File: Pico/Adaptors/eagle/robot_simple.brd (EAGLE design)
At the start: 75.4 x 35.6 mm, 30 parts, among them SW1 3010010P1,MS-22D18,JS202011CQN, U3 MAX1555

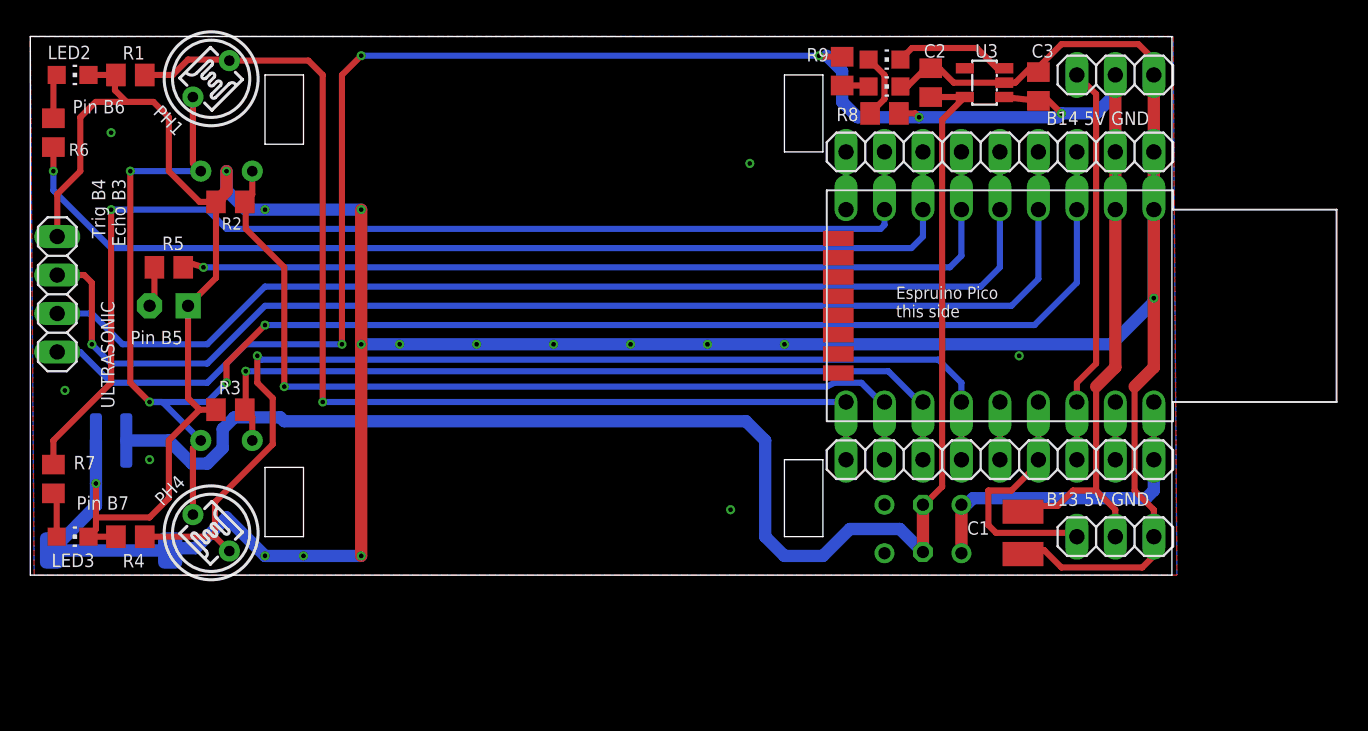
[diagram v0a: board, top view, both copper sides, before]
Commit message: rotate ultrasonic, add fast charge
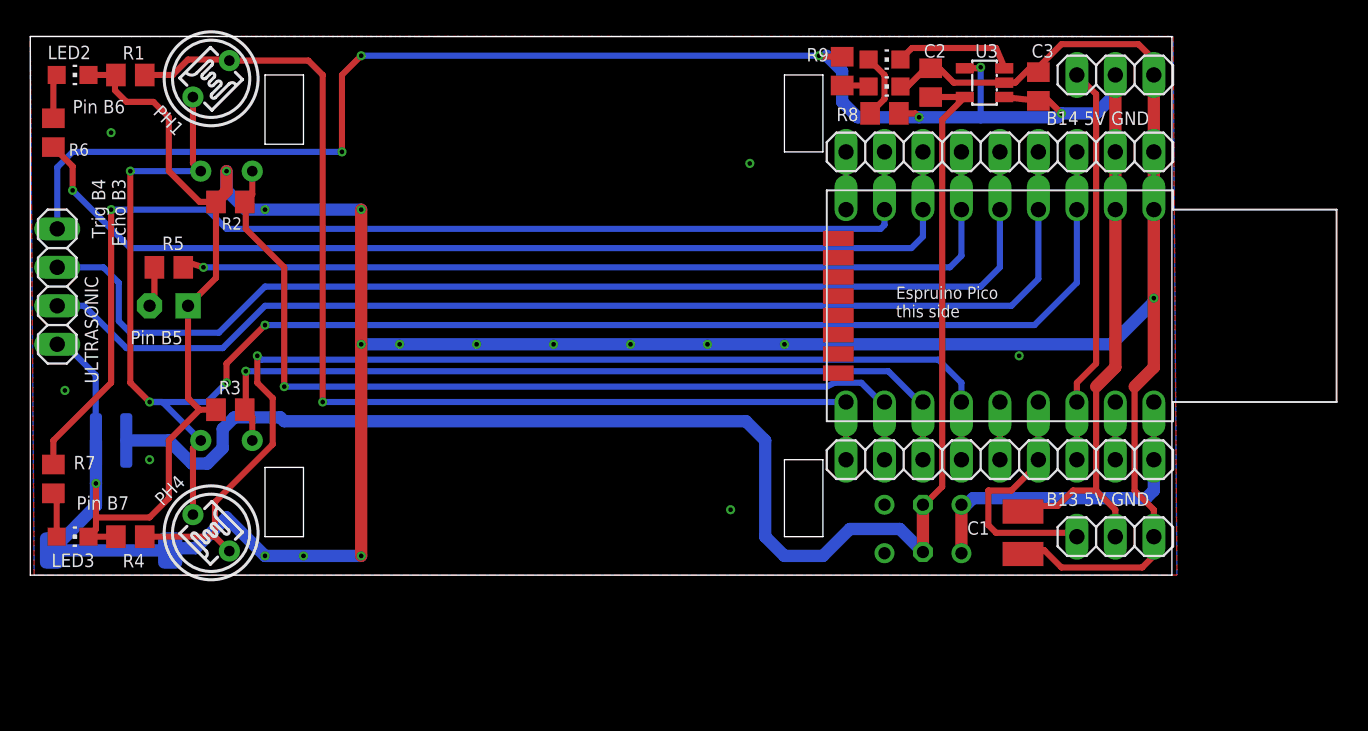
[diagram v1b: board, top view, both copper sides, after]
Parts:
- moved ULTRASONIC 0.51 mm to (1.78, 19.1), turned to 270 degrees
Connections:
- net 5V: now also U3.4
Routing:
- net 5V: track 139.2 -> 133.4 mm, vias 5 -> 6
- net SONIC_ECHO: track 80.3 -> 76.2 mm, vias 1 -> 0
- net SONIC_TRIG: track 72.8 -> 74.9 mm
- net GND: track 249.3 -> 247.8 mm
- net LED2: track 67.7 -> 67.0 mm
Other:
- board text added: "v1.1"
- board text removed: "v1.0"
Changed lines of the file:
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@@
 <text x="4.064" y="26.162" size="0.889" layer="21" rot="R270">Trig B4
 Echo B3</text>
-<text x="40.894" y="25.4" size="0.889" layer="22" rot="MR180">v1.0</text>
+<text x="40.894" y="25.4" size="0.889" layer="22" rot="MR180">v1.1</text>
 </plain>
 <attributes>
@@
 <attribute name="NAME" x="6.096" y="0.508" size="0.889" layer="25"/>
 </element>
-<element name="ULTRASONIC" library="pinhead" package="1X04" value="" x="1.778" y="18.542" smashed="yes" rot="R90">
-<attribute name="NAME" x="5.552515625" y="11.012928125" size="0.889" layer="25" ratio="10" rot="R90"/>
-<attribute name="VALUE" x="4.952996875" y="13.462" size="1.27" layer="27" rot="R90"/>
+<element name="ULTRASONIC" library="pinhead" package="1X04" value="" x="1.778" y="19.05" smashed="yes" rot="R270">
+<attribute name="NAME" x="3.591484375" y="19.721071875" size="0.889" layer="25" ratio="10" rot="R270"/>
+<attribute name="VALUE" x="-1.396996875" y="24.13" size="1.27" layer="27" rot="R270"/>
 </element>
 <element name="J1" library="OPL5" package="2P-SMD-2.0-90D" value="" x="5.334" y="3.81" smashed="yes" rot="MR0"/>
@@
 <wire x1="5.588" y1="32.004" x2="5.588" y2="32.954" width="0.4064" layer="1"/>
 <wire x1="5.588" y1="32.954" x2="5.654" y2="33.02" width="0.4064" layer="1"/>
-<wire x1="1.778" y1="22.352" x2="1.778" y2="25.146" width="0.4064" layer="1"/>
-<wire x1="1.778" y1="25.146" x2="3.302" y2="26.67" width="0.4064" layer="1"/>
-<wire x1="3.302" y1="26.67" x2="3.302" y2="30.226" width="0.4064" layer="1"/>
-<wire x1="3.302" y1="30.226" x2="4.318" y2="31.242" width="0.4064" layer="1"/>
-<wire x1="4.318" y1="31.242" x2="6.35" y2="31.242" width="0.4064" layer="1"/>
 <wire x1="4.334" y1="8.89" x2="4.334" y2="6.053" width="0.8128" layer="16"/>
 <wire x1="4.334" y1="6.053" x2="4.334" y2="4.588" width="0.8128" layer="16"/>
@@
 <via x="7.874" y="7.62" extent="1-16" drill="0.3048"/>
 <via x="5.334" y="29.21" extent="1-16" drill="0.3048"/>
+<wire x1="1.778" y1="15.24" x2="2.286" y2="15.24" width="0.4064" layer="16"/>
+<wire x1="2.286" y1="15.24" x2="4.318" y2="13.208" width="0.4064" layer="16"/>
+<wire x1="4.318" y1="13.208" x2="4.318" y2="6.096" width="0.4064" layer="16"/>
 </signal>
 <signal name="N$5">
@@
 <wire x1="58.42" y1="30.48" x2="58.674" y2="30.226" width="0.4064" layer="1"/>
 <via x="58.674" y="30.226" extent="1-16" drill="0.3048"/>
-<wire x1="58.674" y1="30.226" x2="67.818" y2="30.226" width="0.8128" layer="16"/>
+<wire x1="58.674" y1="30.226" x2="62.738" y2="30.226" width="0.8128" layer="16"/>
+<wire x1="62.738" y1="30.226" x2="67.818" y2="30.226" width="0.8128" layer="16"/>
 <wire x1="67.818" y1="30.226" x2="68.072" y2="30.48" width="0.8128" layer="16"/>
 <wire x1="53.594" y1="34.224" x2="52.136" y2="34.224" width="0.4064" layer="1"/>
@@
 <wire x1="53.594" y1="31.242" x2="54.61" y2="30.226" width="0.8128" layer="16"/>
 <wire x1="54.61" y1="30.226" x2="58.674" y2="30.226" width="0.8128" layer="16"/>
-<wire x1="1.778" y1="14.732" x2="3.302" y2="14.732" width="0.4064" layer="16"/>
-<wire x1="3.302" y1="14.732" x2="5.334" y2="12.7" width="0.4064" layer="16"/>
-<wire x1="5.334" y1="12.7" x2="11.684" y2="12.7" width="0.4064" layer="16"/>
-<wire x1="11.684" y1="12.7" x2="14.224" y2="15.24" width="0.4064" layer="16"/>
-<wire x1="14.224" y1="15.24" x2="20.574" y2="15.24" width="0.4064" layer="16"/>
-<via x="20.574" y="15.24" extent="1-16" drill="0.3048"/>
-<wire x1="20.574" y1="15.24" x2="20.574" y2="33.02" width="0.4064" layer="1"/>
 <wire x1="20.574" y1="33.02" x2="21.844" y2="34.29" width="0.4064" layer="1"/>
 <via x="21.844" y="34.29" extent="1-16" drill="0.3048"/>
 <wire x1="21.844" y1="34.29" x2="52.07" y2="34.29" width="0.4064" layer="16"/>
+<contactref element="U3" pad="4"/>
+<wire x1="61.6919" y1="33.462" x2="62.672" y2="33.462" width="0.4064" layer="1"/>
+<wire x1="62.672" y1="33.462" x2="62.738" y2="33.528" width="0.4064" layer="1"/>
+<via x="62.738" y="33.528" extent="1-16" drill="0.3048"/>
+<wire x1="62.738" y1="33.528" x2="62.738" y2="30.226" width="0.4064" layer="16"/>
+<wire x1="20.574" y1="33.02" x2="20.574" y2="27.94" width="0.4064" layer="1"/>
+<via x="20.574" y="27.94" extent="1-16" drill="0.3048"/>
+<wire x1="20.574" y1="27.94" x2="2.794" y2="27.94" width="0.4064" layer="16"/>
+<wire x1="2.794" y1="27.94" x2="1.778" y2="26.924" width="0.4064" layer="16"/>
+<wire x1="1.778" y1="26.924" x2="1.778" y2="22.86" width="0.4064" layer="16"/>
 </signal>
 <signal name="LDR1">
@@
 <wire x1="66.548" y1="19.558" x2="64.77" y2="17.78" width="0.4064" layer="16"/>
 <wire x1="64.77" y1="17.78" x2="15.494" y2="17.78" width="0.4064" layer="16"/>
-<wire x1="15.494" y1="17.78" x2="11.684" y2="13.97" width="0.4064" layer="16"/>
-<wire x1="11.684" y1="13.97" x2="5.334" y2="13.97" width="0.4064" layer="16"/>
-<wire x1="5.334" y1="13.97" x2="4.064" y2="15.24" width="0.4064" layer="16"/>
-<via x="4.064" y="15.24" extent="1-16" drill="0.3048"/>
-<wire x1="4.064" y1="15.24" x2="4.064" y2="19.304" width="0.4064" layer="1"/>
-<wire x1="4.064" y1="19.304" x2="3.556" y2="19.812" width="0.4064" layer="1"/>
-<wire x1="3.556" y1="19.812" x2="1.778" y2="19.812" width="0.4064" layer="1"/>
+<wire x1="15.494" y1="17.78" x2="12.7" y2="14.986" width="0.4064" layer="16"/>
+<wire x1="12.7" y1="14.986" x2="6.35" y2="14.986" width="0.4064" layer="16"/>
+<wire x1="6.35" y1="14.986" x2="3.556" y2="17.78" width="0.4064" layer="16"/>
+<wire x1="3.556" y1="17.78" x2="1.778" y2="17.78" width="0.4064" layer="16"/>
 </signal>
 <signal name="SONIC_TRIG">
@@
 <wire x1="64.008" y1="20.32" x2="62.738" y2="19.05" width="0.4064" layer="16"/>
 <wire x1="62.738" y1="19.05" x2="15.494" y2="19.05" width="0.4064" layer="16"/>
-<wire x1="15.494" y1="19.05" x2="11.684" y2="15.24" width="0.4064" layer="16"/>
-<wire x1="11.684" y1="15.24" x2="6.096" y2="15.24" width="0.4064" layer="16"/>
-<wire x1="6.096" y1="15.24" x2="4.064" y2="17.272" width="0.4064" layer="16"/>
-<wire x1="4.064" y1="17.272" x2="1.778" y2="17.272" width="0.4064" layer="16"/>
+<wire x1="15.494" y1="19.05" x2="12.446" y2="16.002" width="0.4064" layer="16"/>
+<wire x1="12.446" y1="16.002" x2="6.604" y2="16.002" width="0.4064" layer="16"/>
+<wire x1="6.604" y1="16.002" x2="5.842" y2="16.764" width="0.4064" layer="16"/>
+<wire x1="5.842" y1="16.764" x2="5.842" y2="19.304" width="0.4064" layer="16"/>
+<wire x1="5.842" y1="19.304" x2="4.826" y2="20.32" width="0.4064" layer="16"/>
+<wire x1="4.826" y1="20.32" x2="1.778" y2="20.32" width="0.4064" layer="16"/>
 </signal>
 <signal name="3.3V" class="1">
@@
 <contactref element="LED4" pad="C"/>
 <contactref element="U3" pad="3"/>
-<wire x1="64.2921" y1="33.462" x2="63.82" y2="33.462" width="0.4064" layer="1"/>
-<wire x1="63.82" y1="33.462" x2="62.484" y2="34.798" width="0.4064" layer="1"/>
-<wire x1="62.484" y1="34.798" x2="58.2" y2="34.798" width="0.4064" layer="1"/>
+<wire x1="64.2921" y1="33.462" x2="64.328" y2="33.462" width="0.4064" layer="1"/>
+<wire x1="64.328" y1="33.462" x2="63.754" y2="34.798" width="0.4064" layer="1"/>
+<wire x1="63.754" y1="34.798" x2="58.2" y2="34.798" width="0.4064" layer="1"/>
 <wire x1="58.2" y1="34.798" x2="57.438" y2="34.036" width="0.4064" layer="1"/>
 </signal>
@@
 <wire x1="58.928" y1="24.13" x2="58.928" y2="22.352" width="0.4064" layer="16"/>
 <wire x1="58.928" y1="22.352" x2="58.166" y2="21.59" width="0.4064" layer="16"/>
-<wire x1="58.166" y1="21.59" x2="5.334" y2="21.59" width="0.4064" layer="16"/>
-<wire x1="5.334" y1="21.59" x2="1.524" y2="25.4" width="0.4064" layer="16"/>
-<wire x1="1.524" y1="25.4" x2="1.524" y2="26.67" width="0.4064" layer="16"/>
-<via x="1.524" y="26.67" extent="1-16" drill="0.3048"/>
-<wire x1="1.524" y1="26.67" x2="1.524" y2="28.26" width="0.4064" layer="1"/>
+<wire x1="58.166" y1="21.59" x2="6.604" y2="21.59" width="0.4064" layer="16"/>
+<wire x1="6.604" y1="21.59" x2="2.794" y2="25.4" width="0.4064" layer="16"/>
+<via x="2.794" y="25.4" extent="1-16" drill="0.3048"/>
+<wire x1="1.524" y1="28.26" x2="2.794" y2="26.99" width="0.4064" layer="1"/>
+<wire x1="2.794" y1="26.99" x2="2.794" y2="25.4" width="0.4064" layer="1"/>
 </signal>
 <signal name="N$2">

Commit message: tweaked robot design - swap LEDs, add optional bluetooth
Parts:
- added U1: HC_05, bluetooth:BLUETOOTH_SMD
- U$1: value ESPRUINO_PICO_HALFSMD -> ESPRUINO_PICO_0.1; device espruino_pico:ESPRUINO_PICO_HALFSMD -> espruino_pico:ESPRUINO_PICO_0.1
- renumbered LED1 to LED_MID, LED2 to LED_RIGHT, LED3 to LED_LEFT, PH1 to LDR1, PH2 to LDR2, PH3 to LDR3, PH4 to LDR4
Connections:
- net LED1 renamed LED_MID
- removed net $N52: JP5.5, U$1.B10
- removed net LED2: J3.3, R6.2, U$1.B6
- removed net LED3: J3.2, R7.2, U$1.B7
- removed net N$1: J3.1, U$1.A8
- new net BT_RX: J3.3, U$1.B6, U1.2
- new net BT_TX: J3.2, U$1.B7, U1.1
- new net LED_LEFT: J3.1, R7.2, U$1.A8
- new net LED_RIGHT: JP5.5, R6.2, U$1.B10
- net 3.3V: now also U1.12
- net GND: now also U1.13, U1.14, U1.21, U1.22
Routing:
- net LED_RIGHT: track 0.00 -> 78.7 mm, vias 0 -> 2
- net LED3: track 74.9 -> 0.00 mm, vias 1 -> 0
- net LED_LEFT: track 0.00 -> 72.2 mm, vias 0 -> 1
- net LED2: track 67.0 -> 0.00 mm, vias 1 -> 0
- net BT_RX: track 0.00 -> 37.4 mm
- net BT_TX: track 0.00 -> 36.5 mm, vias 0 -> 2
- net N$1: track 3.81 -> 0.00 mm
- net $N52: track 3.81 -> 0.00 mm
- net 3.3V: track 108.9 -> 111.2 mm, vias 4 -> 5
- net LED_MID: track 58.7 -> 60.9 mm
- net GND: vias 21 -> 20
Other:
- board text added: "Pin A8"
- board text added: "Pin B10"
- board text removed: "Pin B6"
- board text removed: "Pin B7"
